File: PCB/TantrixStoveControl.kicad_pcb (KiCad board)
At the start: 2 copper layers, 25.8 x 75 mm, 16 parts, among them J1 6P6C, U1 PC817, U2 PC817, U2 WeMos_mini, U4 PC817

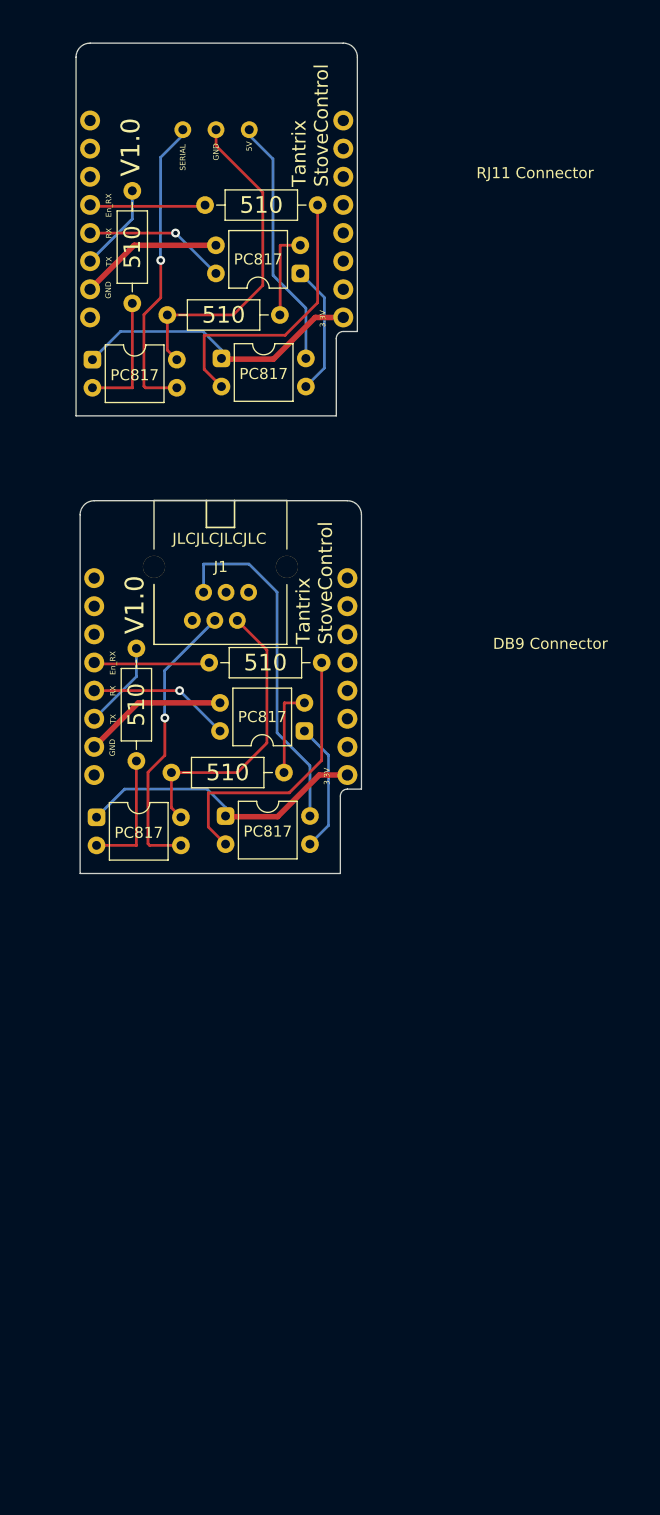
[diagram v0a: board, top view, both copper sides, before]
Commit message: New PCB project designed. Check it on KiCad
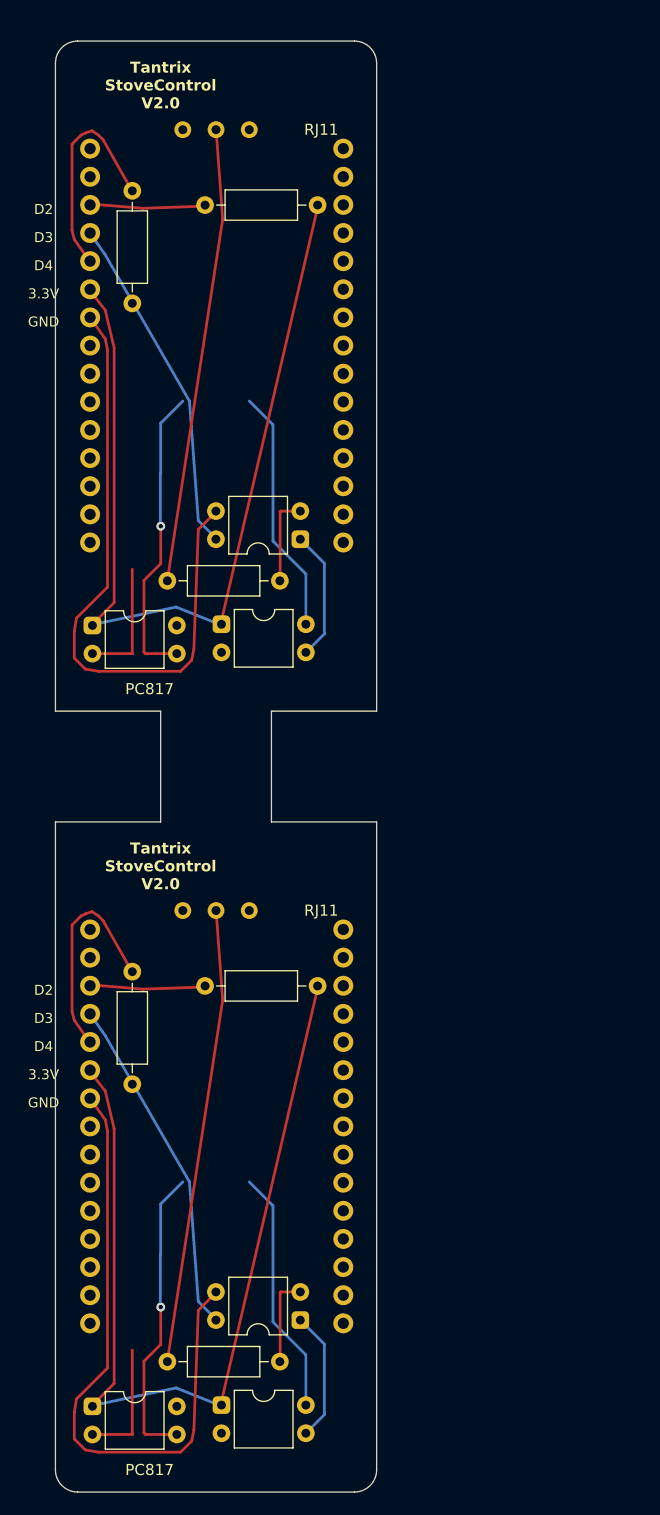
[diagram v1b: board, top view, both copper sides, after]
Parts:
- removed the R1 at (34.9, 75.6)
- removed the R1 at (31.5, 85.5)
- removed the U2 at (43.5, 81.8)
- removed the U2 at (35.6, 35.6)
- removed the U2 at (35.9, 76.9)
- added R1: 500, Resistor_THT:R_Axial_DIN0207_L6.3mm_D2.5mm_P10.16mm_Horizontal, F.Cu at (34.5, 104.8)
- added R1: 500, Resistor_THT:R_Axial_DIN0207_L6.3mm_D2.5mm_P10.16mm_Horizontal, F.Cu at (31.1, 138.7)
- added U2: NodeMCU_Amica_V2, nodemcu_amica_v2:NodeMCU_Amica_V2_DIL, B.Cu at (35.6, 47.0)
- added U2: PC817, Package_DIP:DIP-4_W7.62mm, F.Cu at (43.1, 135.0)
- added U2: NodeMCU_Amica_V2, nodemcu_amica_v2:NodeMCU_Amica_V2_DIL, B.Cu at (35.6, 117.5)
- moved U1 53.2 mm to (36.0, 142.7)
- moved U4 53.2 mm to (24.3, 142.8)
- moved R3 29.2 mm to (27.9, 103.5)
- moved J1 29.1 mm to (34.5, 96.0)
- moved R1 24.0 mm to (31.1, 68.2)
- moved U1 24.0 mm to (36.0, 72.2)
- moved U2 24.0 mm to (43.1, 64.5)
- moved U4 24.0 mm to (24.3, 72.3)
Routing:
- net (no net): track 420.3 -> 646.5 mm, vias 4 -> 2
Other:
- board size 25.8 x 75 mm -> 29 x 131 mm
- board text added: "D2"
- board text added: "D3"
- board text added: "D4"
- board text added: "RJ11"
- board text added: "Tantrix StoveControl V2.0"
- board text removed: "510"
- board text removed: "5V"
- board text removed: "DB9 Connector"
- board text removed: "En_RX"
- board text removed: "JLCJLCJLCJLC"
- board text removed: "RJ11 Connector"
- board text removed: "RX"
- board text removed: "SERIAL"
- board text removed: "TX"
- board text removed: "Tantrix StoveControl"
- board text removed: "Tantrix StoveControl V1.0"
- board text removed: "V1.0"
